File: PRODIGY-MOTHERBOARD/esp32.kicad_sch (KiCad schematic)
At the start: 3 parts, among them U2 CP2102N-Axx-xQFN24, U3 ESP32-WROOM-32

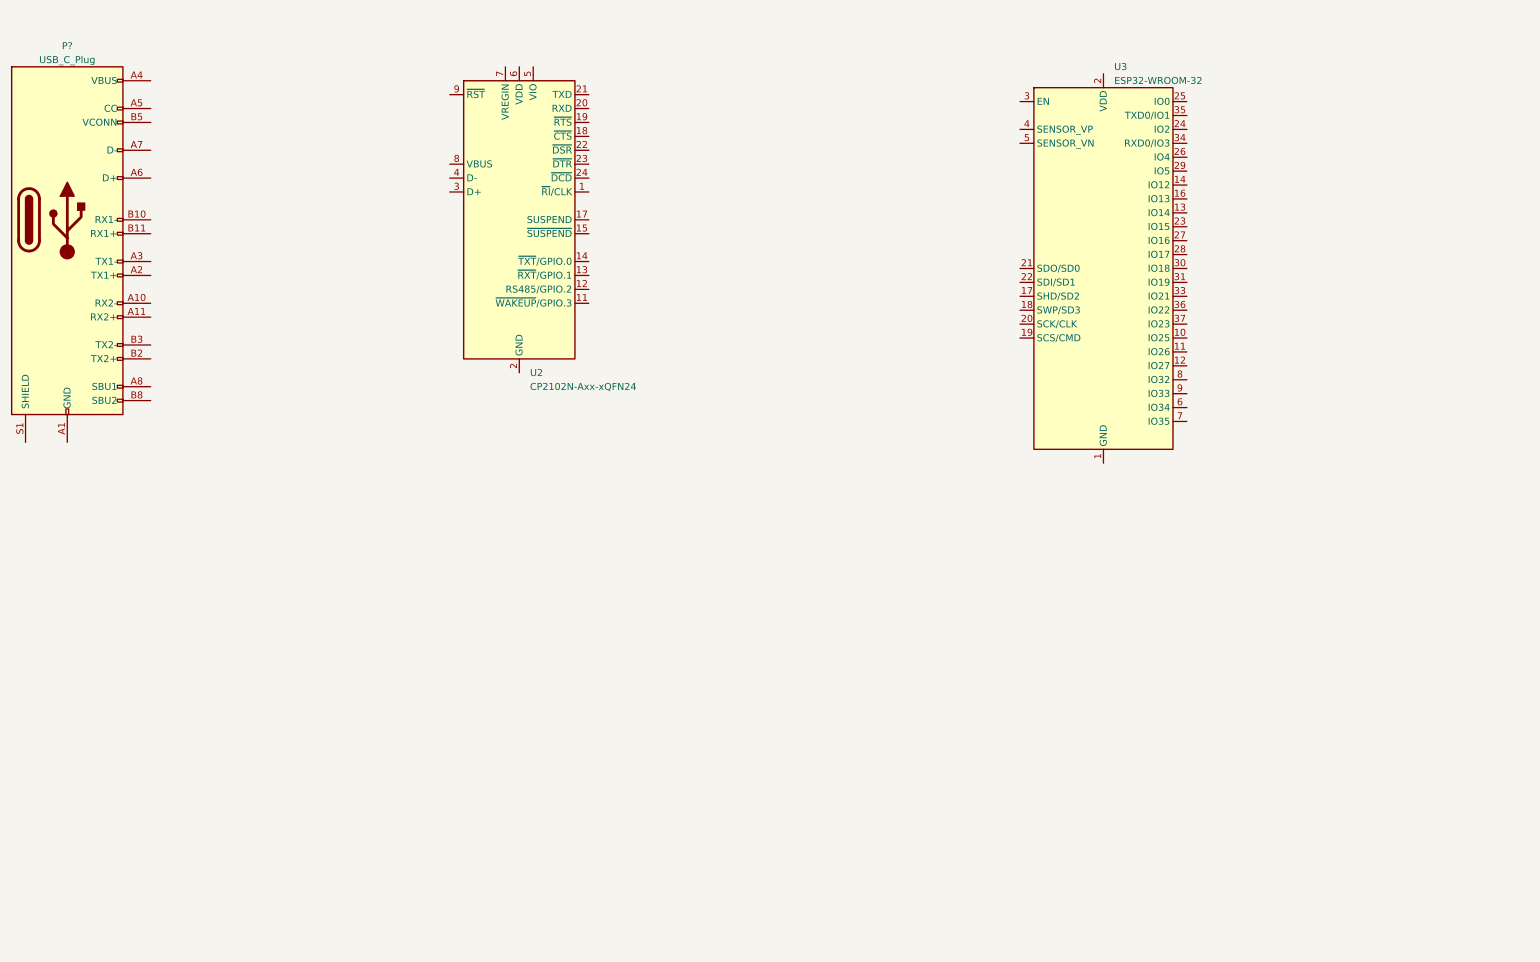
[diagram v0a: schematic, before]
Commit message: project restructure done. Hierarchical sheet done. Outputs/breakouts sheet done
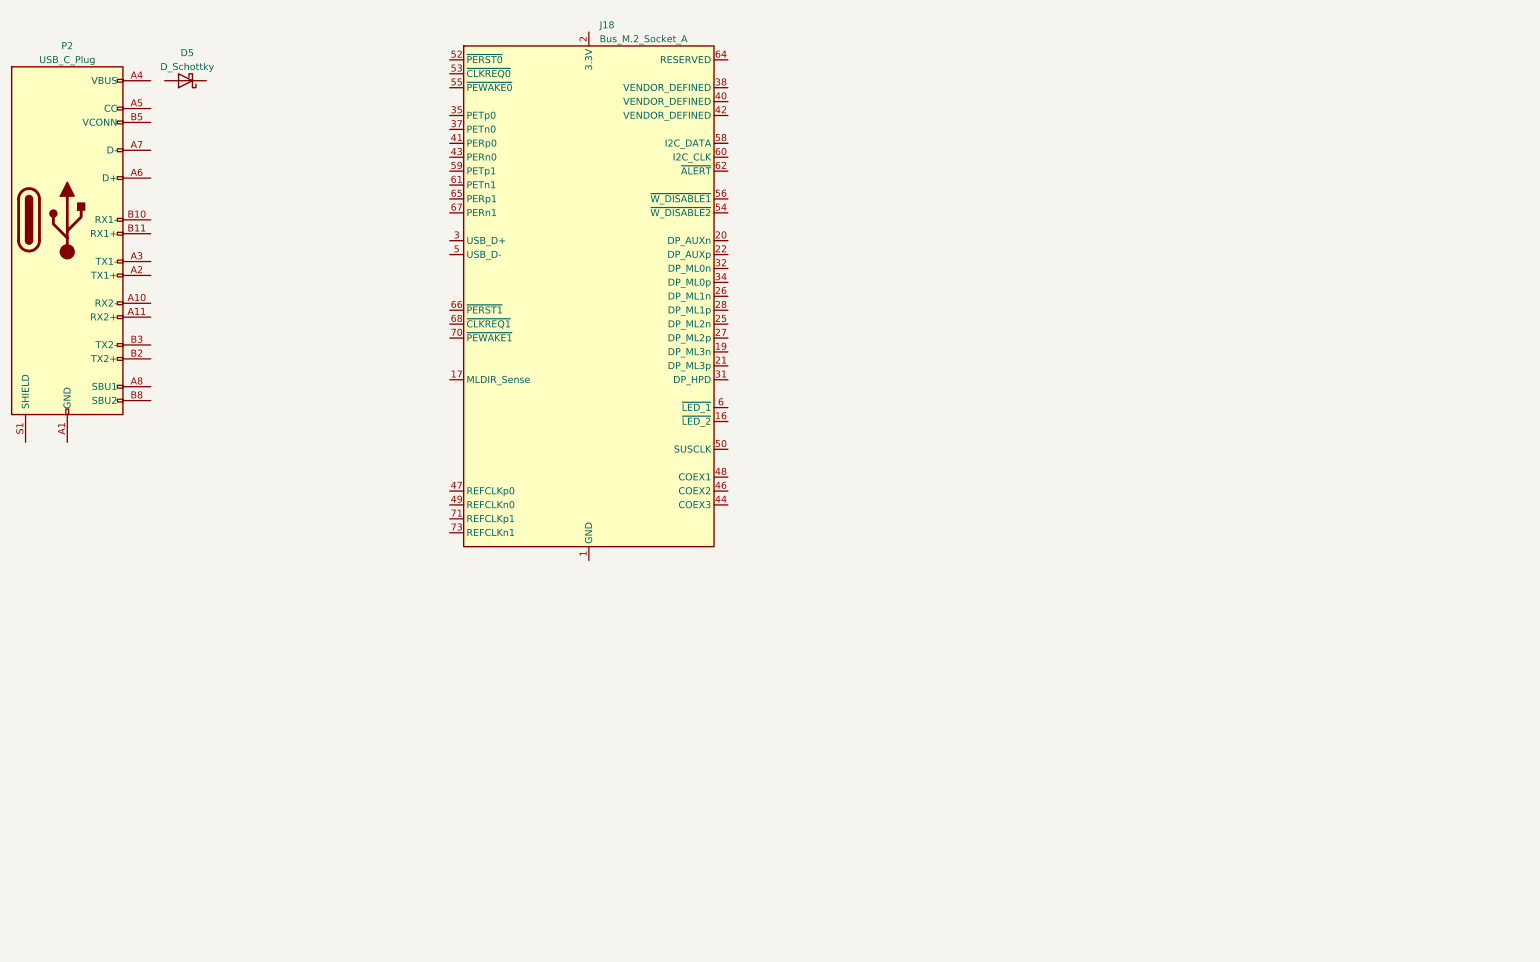
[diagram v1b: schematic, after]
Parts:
- removed U2: CP2102N-Axx-xQFN24, Package_DFN_QFN:QFN-24-1EP_4x4mm_P0.5mm_EP2.6x2.6mm, symbol Interface_USB:CP2102N-Axx-xQFN24
- removed U3: ESP32-WROOM-32, RF_Module:ESP32-WROOM-32, symbol RF_Module:ESP32-WROOM-32
- added D5: D_Schottky, Diode_SMD:D_SMB, symbol Device:D_Schottky
- added J18: Bus_M.2_Socket_A, m.2_edge_connector_key_a:121992304, symbol Connector:Bus_M.2_Socket_A
- gave numbers to parts that had none: 1
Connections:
- new net: J18.1 (GND), J18.18 (GND), J18.23 (GND), J18.24 (GND), J18.29 (GND), J18.30 (GND), J18.33 (GND), J18.36 (GND), J18.39 (GND), J18.45 (GND), J18.51 (GND), J18.57 (GND), J18.63 (GND), J18.69 (GND), J18.7 (GND), J18.75 (GND)
- new net: J18.2 (3.3V), J18.4 (3.3V), J18.72 (3.3V), J18.74 (3.3V)

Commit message: CAN schematic done
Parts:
- removed J18: Bus_M.2_Socket_A, m.2_edge_connector_key_a:121992304, symbol Connector:Bus_M.2_Socket_A
- added C57: 100nF, symbol Device:C
- added J2: Bus_M.2_Socket_B, symbol Connector:Bus_M.2_Socket_B
- added R65: 10k, Resistor_SMD:R_0603_1608Metric, symbol Device:R
- added R66: 100, Resistor_SMD:R_0603_1608Metric, symbol Device:R
- added SW6: SW_Push_Dual_x2, symbol Switch:SW_Push_Dual_x2
- renumbered D5 to D7, P2 to P1
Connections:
- net +5V: now reaches D7.1 (K)
- net at D7.2 (A): now also P1.A4 (VBUS), P1.A9 (VBUS), P1.B4 (VBUS), P1.B9 (VBUS)
- new net: R65.1, R66.1, SW6.2 (D), SW6.4 (D)
- new net: J2.11 (GND), J2.27 (GND), J2.3 (GND), J2.33 (GND), J2.39 (GND), J2.45 (GND), J2.5 (GND), J2.51 (GND), J2.57 (GND), J2.71 (GND), J2.73 (GND)
- new net: J2.2 (3.3V), J2.4 (3.3V), J2.70 (3.3V), J2.72 (3.3V), J2.74 (3.3V)
- new net +3V3: R65.2
- new net ESP_BUTTON_RESET: C57.1, J2.67 (~{RESET}), R66.2
- new net GND: C57.2, SW6.1 (C), SW6.3 (C)

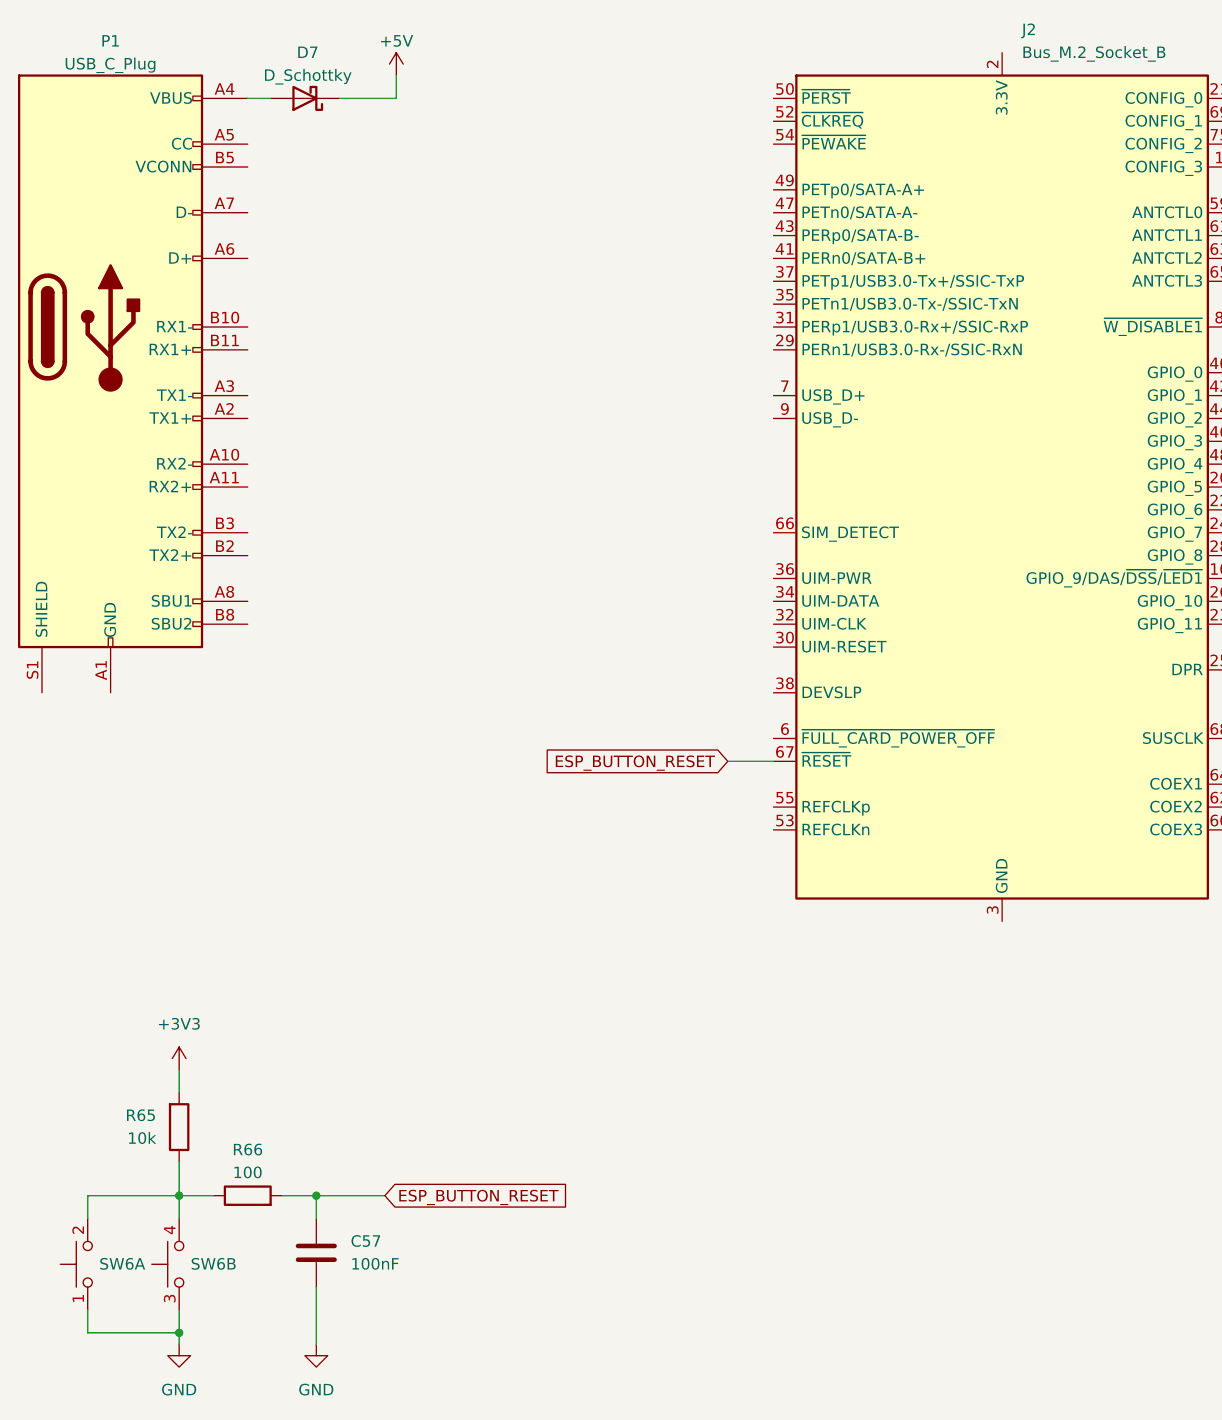
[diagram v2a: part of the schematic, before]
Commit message: SPI NFC schematic done.
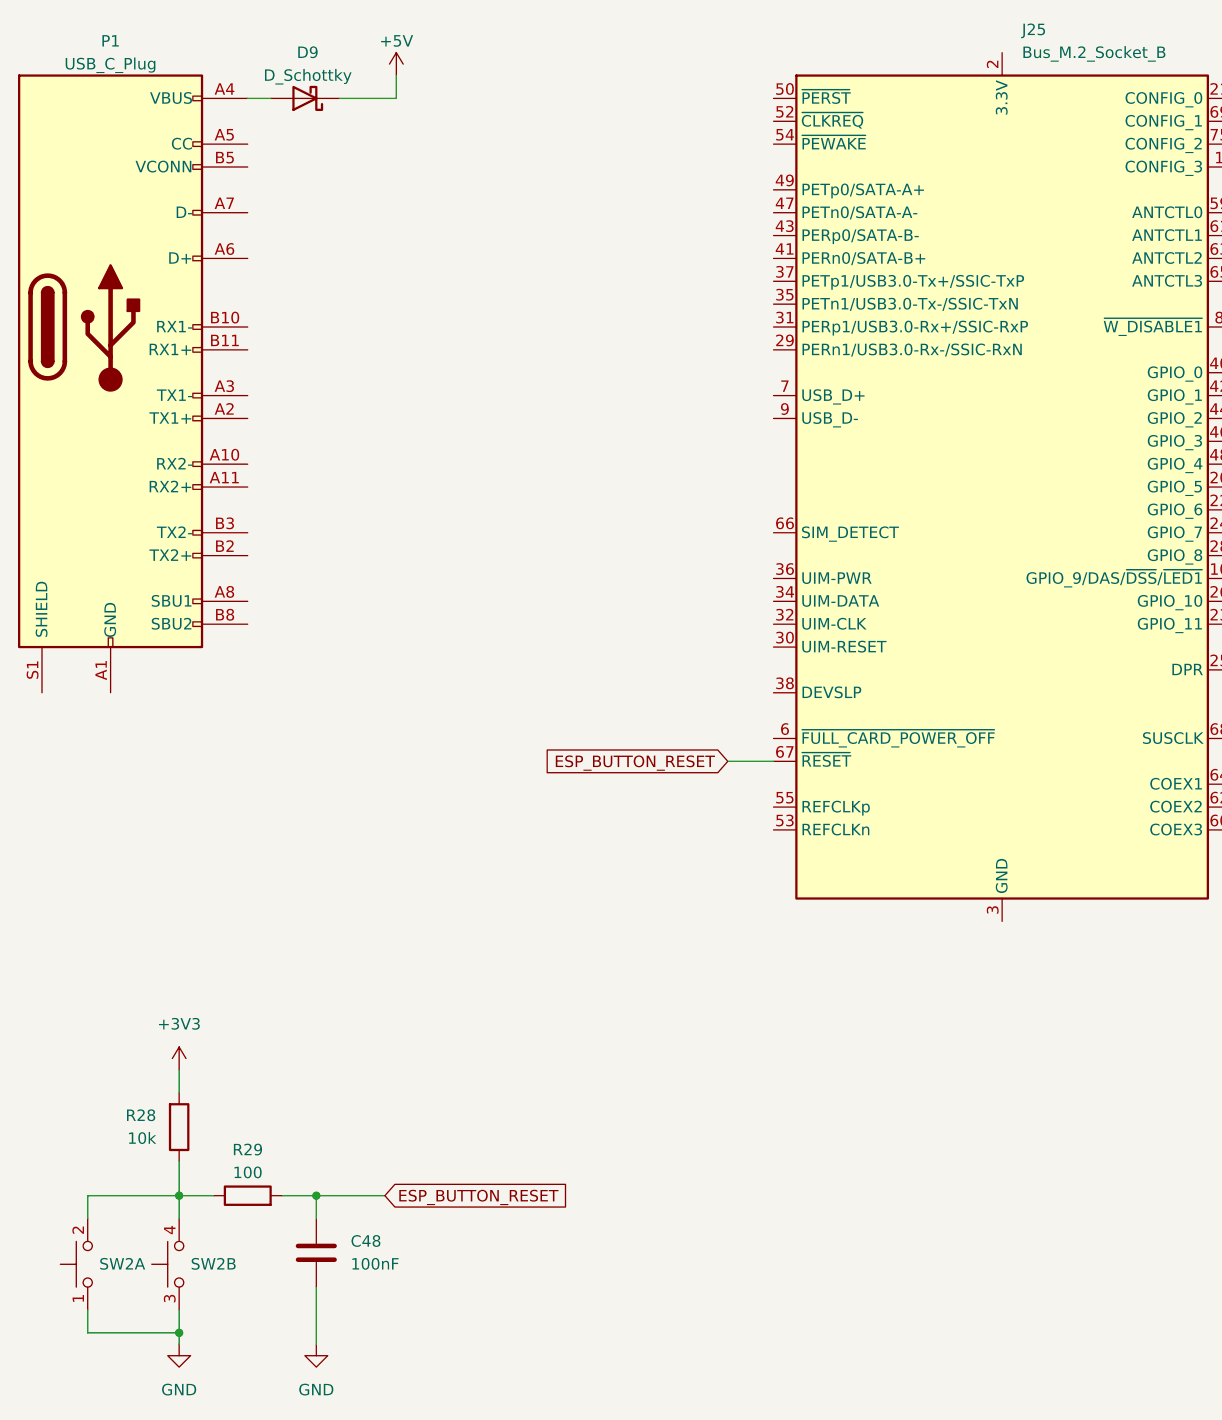
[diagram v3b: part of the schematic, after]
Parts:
- renumbered C57 to C48, D7 to D9, J2 to J25, R65 to R28, R66 to R29, SW6 to SW2
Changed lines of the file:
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@@
 		(dnp no)
 		(fields_autoplaced yes)
-		(property "Reference" "#PWR0147"
+		(property "Reference" "#PWR068"
 			(at 39.37 177.8 0)
 			(effects
@@
 			(project "PRODIGY-MOTHERBOARD"
 				(path "/f1c25860-8989-4190-bd24-2491d23ca7d9/4747deee-8806-443e-847a-65f550cadde4"
-					(reference "#PWR0147")
+					(reference "#PWR068")
 					(unit 1)
 				)
@@
 		(dnp no)
 		(fields_autoplaced yes)
-		(property "Reference" "#PWR0149"
+		(property "Reference" "#PWR070"
 			(at 63.5 34.29 0)
 			(effects
@@
 			(project "PRODIGY-MOTHERBOARD"
 				(path "/f1c25860-8989-4190-bd24-2491d23ca7d9/4747deee-8806-443e-847a-65f550cadde4"
-					(reference "#PWR0149")
+					(reference "#PWR070")
 					(unit 1)
 				)
@@
 		(dnp no)
 		(fields_autoplaced yes)
-		(property "Reference" "D7"
+		(property "Reference" "D9"
 			(at 53.6575 27.94 0)
 			(effects
@@
 			(project "PRODIGY-MOTHERBOARD"
 				(path "/f1c25860-8989-4190-bd24-2491d23ca7d9/4747deee-8806-443e-847a-65f550cadde4"
-					(reference "D7")
+					(reference "D9")
 					(unit 1)
 				)
@@
 		(dnp no)
 		(fields_autoplaced yes)
-		(property "Reference" "C57"
+		(property "Reference" "C48"
 			(at 58.42 160.0199 0)
 			(effects
@@
 			(project "PRODIGY-MOTHERBOARD"
 				(path "/f1c25860-8989-4190-bd24-2491d23ca7d9/4747deee-8806-443e-847a-65f550cadde4"
-					(reference "C57")
+					(reference "C48")
 					(unit 1)
 				)
@@
 		(dnp no)
 		(fields_autoplaced yes)
-		(property "Reference" "R66"
+		(property "Reference" "R29"
 			(at 46.99 149.86 90)
 			(effects
@@
 			(project "PRODIGY-MOTHERBOARD"
 				(path "/f1c25860-8989-4190-bd24-2491d23ca7d9/4747deee-8806-443e-847a-65f550cadde4"
-					(reference "R66")
+					(reference "R29")
 					(unit 1)
 				)
@@
 		(dnp no)
 		(fields_autoplaced yes)
-		(property "Reference" "#PWR0146"
+		(property "Reference" "#PWR067"
 			(at 39.37 144.78 0)
 			(effects
@@
 			(project "PRODIGY-MOTHERBOARD"
 				(path "/f1c25860-8989-4190-bd24-2491d23ca7d9/4747deee-8806-443e-847a-65f550cadde4"
-					(reference "#PWR0146")
+					(reference "#PWR067")
 					(unit 1)
 				)
@@
 		(dnp no)
 		(fields_autoplaced yes)
-		(property "Reference" "SW6"
+		(property "Reference" "SW2"
 			(at 40.64 162.5599 90)
 			(effects
@@
 			(project "PRODIGY-MOTHERBOARD"
 				(path "/f1c25860-8989-4190-bd24-2491d23ca7d9/4747deee-8806-443e-847a-65f550cadde4"
-					(reference "SW6")
+					(reference "SW2")
 					(unit 2)
 				)
@@
 		(on_board yes)
 		(dnp no)
-		(property "Reference" "R65"
+		(property "Reference" "R28"
 			(at 36.83 146.0499 0)
 			(effects
@@
 			(project "PRODIGY-MOTHERBOARD"
 				(path "/f1c25860-8989-4190-bd24-2491d23ca7d9/4747deee-8806-443e-847a-65f550cadde4"
-					(reference "R65")
+					(reference "R28")
 					(unit 1)
 				)
@@
 		(dnp no)
 		(fields_autoplaced yes)
-		(property "Reference" "SW6"
+		(property "Reference" "SW2"
 			(at 30.48 162.5599 90)
 			(effects
@@
 			(project "PRODIGY-MOTHERBOARD"
 				(path "/f1c25860-8989-4190-bd24-2491d23ca7d9/4747deee-8806-443e-847a-65f550cadde4"
-					(reference "SW6")
+					(reference "SW2")
 					(unit 1)
 				)
@@
 		(dnp no)
 		(fields_autoplaced yes)
-		(property "Reference" "#PWR0148"
+		(property "Reference" "#PWR069"
 			(at 54.61 177.8 0)
 			(effects
@@
 			(project "PRODIGY-MOTHERBOARD"
 				(path "/f1c25860-8989-4190-bd24-2491d23ca7d9/4747deee-8806-443e-847a-65f550cadde4"
-					(reference "#PWR0148")
+					(reference "#PWR069")
 					(unit 1)
 				)
@@
 		(dnp no)
 		(fields_autoplaced yes)
-		(property "Reference" "J2"
+		(property "Reference" "J25"
 			(at 133.0041 25.4 0)
 			(effects
@@
 			(project "PRODIGY-MOTHERBOARD"
 				(path "/f1c25860-8989-4190-bd24-2491d23ca7d9/4747deee-8806-443e-847a-65f550cadde4"
-					(reference "J2")
-					(unit 1)
-				)
+					(reference "J25")
+					(unit 1)
+				)
